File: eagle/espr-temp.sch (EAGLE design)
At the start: 34 parts, among them IC1 FT231XS-R, IC2 ESP-WROOM-02, IC3 AM2320

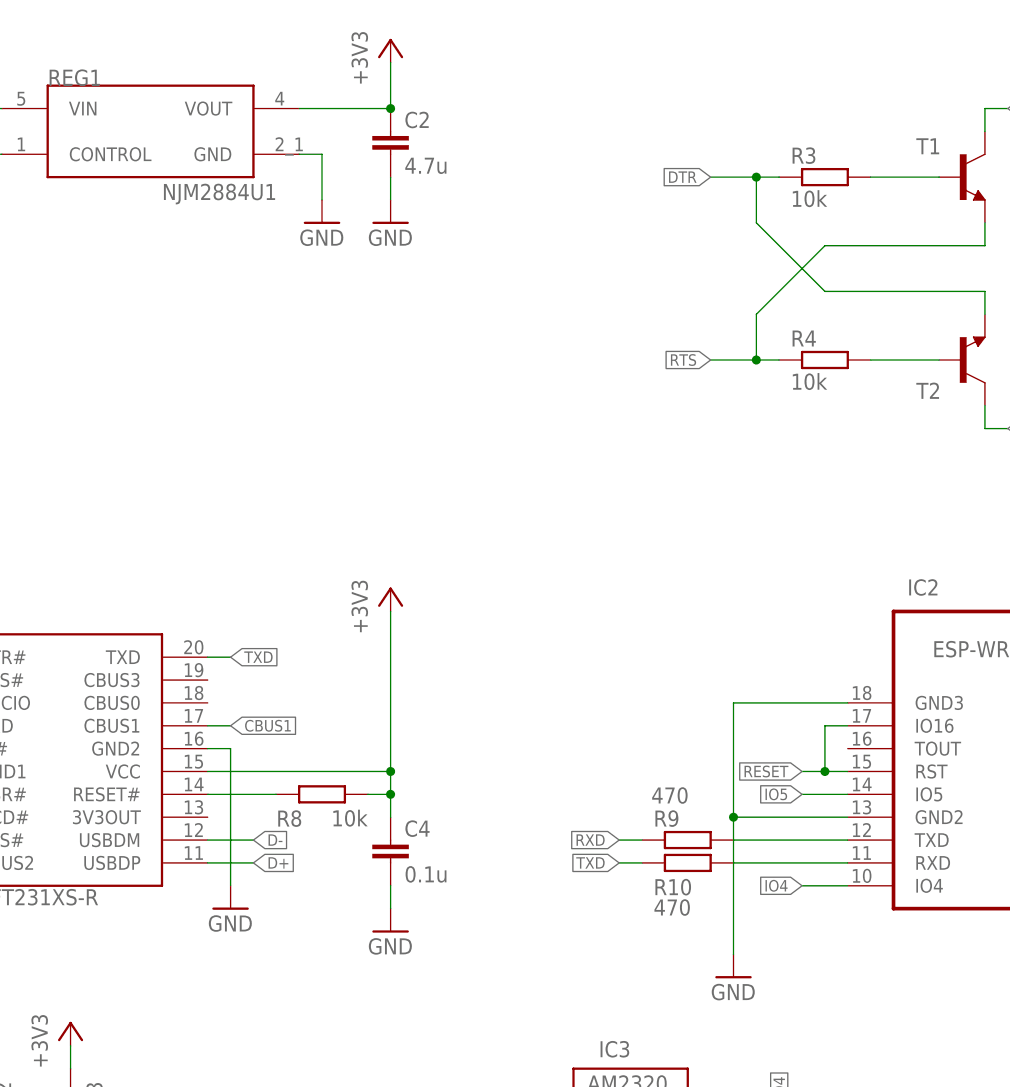
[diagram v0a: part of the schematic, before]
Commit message: fix some ERC errors
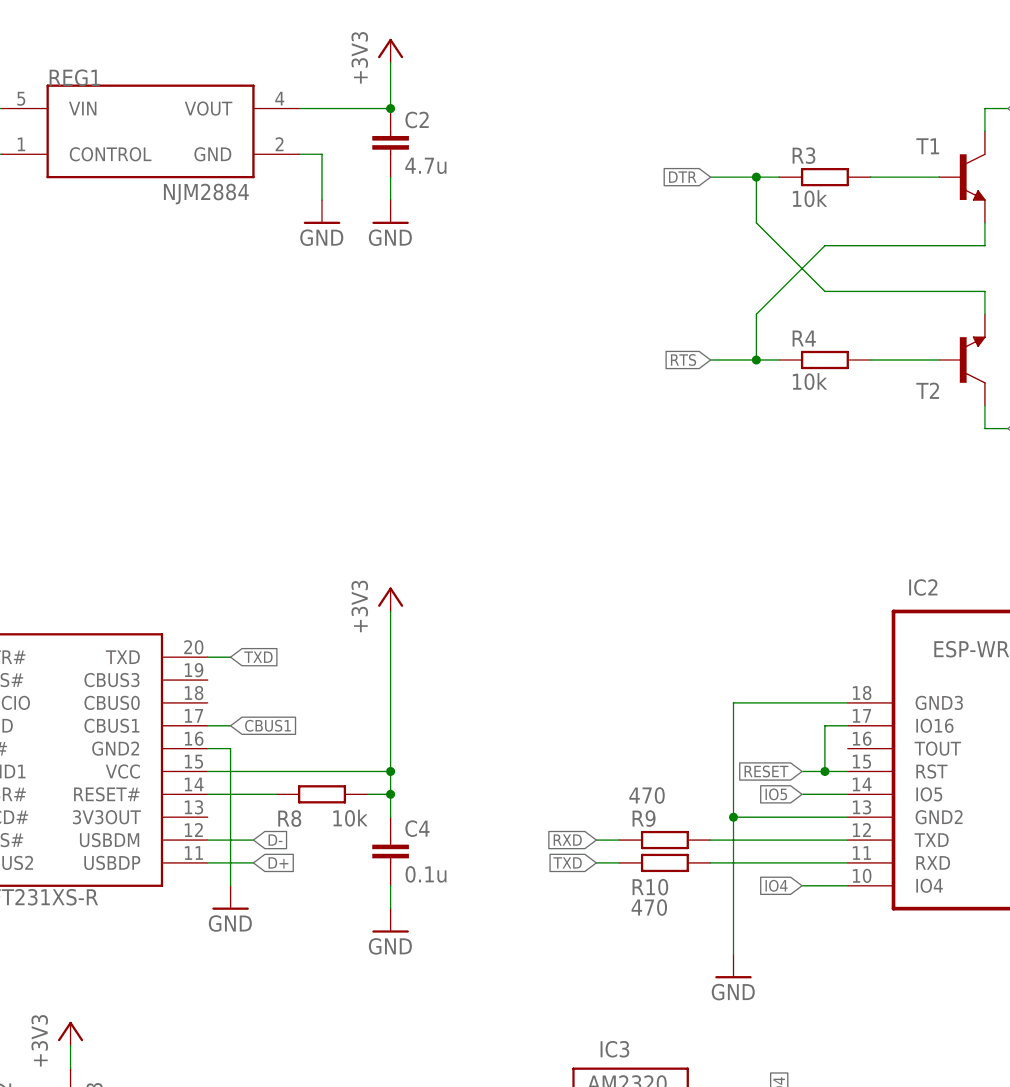
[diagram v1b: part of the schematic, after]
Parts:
- REG1: value NJM2884U1 -> NJM2884; device regulator:NJM2884U1 -> regulator:NJM2884
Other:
- moved on the sheet: R10, R9, REG1
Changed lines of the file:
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@@
 <part name="+3V32" library="supply1" library_urn="urn:adsk.eagle:library:371" deviceset="+3V3" device=""/>
 <part name="+3V33" library="supply1" library_urn="urn:adsk.eagle:library:371" deviceset="+3V3" device=""/>
-<part name="FRAME1" library="frames" library_urn="urn:adsk.eagle:library:229" deviceset="A4L-LOC" device=""/>
-<part name="REG1" library="regulator" deviceset="NJM2884U1" device=""/>
+<part name="FRAME1" library="frames" library_urn="urn:adsk.eagle:library:229" deviceset="A4L-LOC" device="" value="Frame"/>
+<part name="REG1" library="regulator" deviceset="NJM2884" device=""/>
 </parts>
 <sheets>
@@
 <attribute name="VALUE" x="58.674" y="13.081" size="1.778" layer="96"/>
 </instance>
-<instance part="R9" gate="G$1" x="10.16" y="-15.24" smashed="yes">
-<attribute name="NAME" x="6.35" y="-13.7414" size="1.778" layer="95"/>
-<attribute name="VALUE" x="6.096" y="-11.176" size="1.778" layer="96"/>
+<instance part="R9" gate="G$1" x="7.62" y="-15.24" smashed="yes">
+<attribute name="NAME" x="3.81" y="-13.7414" size="1.778" layer="95"/>
+<attribute name="VALUE" x="3.556" y="-11.176" size="1.778" layer="96"/>
 </instance>
 <instance part="R3" gate="G$1" x="25.4" y="58.42"/>
 <instance part="R4" gate="G$1" x="25.4" y="38.1"/>
-<instance part="R10" gate="G$1" x="10.16" y="-17.78" smashed="yes">
-<attribute name="NAME" x="6.35" y="-21.3614" size="1.778" layer="95"/>
-<attribute name="VALUE" x="6.35" y="-23.622" size="1.778" layer="96"/>
+<instance part="R10" gate="G$1" x="7.62" y="-17.78" smashed="yes">
+<attribute name="NAME" x="3.81" y="-21.3614" size="1.778" layer="95"/>
+<attribute name="VALUE" x="3.81" y="-23.622" size="1.778" layer="96"/>
 </instance>
 <instance part="GND1" gate="1" x="-30.48" y="53.34"/>
@@
 <segment>
 <pinref part="R10" gate="G$1" pin="1"/>
-<wire x1="5.08" y1="-17.78" x2="2.54" y2="-17.78" width="0.1524" layer="91"/>
-<label x="2.54" y="-17.78" size="1.27" layer="95" rot="R180" xref="yes"/>
+<wire x1="2.54" y1="-17.78" x2="0" y2="-17.78" width="0.1524" layer="91"/>
+<label x="0" y="-17.78" size="1.27" layer="95" rot="R180" xref="yes"/>
 </segment>
 </net>
@@
 <segment>
 <pinref part="R9" gate="G$1" pin="1"/>
-<wire x1="5.08" y1="-15.24" x2="2.54" y2="-15.24" width="0.1524" layer="91"/>
-<label x="2.54" y="-15.24" size="1.27" layer="95" rot="R180" xref="yes"/>
+<wire x1="2.54" y1="-15.24" x2="0" y2="-15.24" width="0.1524" layer="91"/>
+<label x="0" y="-15.24" size="1.27" layer="95" rot="R180" xref="yes"/>
 </segment>
 </net>
@@
 <pinref part="R9" gate="G$1" pin="2"/>
 <pinref part="IC2" gate="G$1" pin="TXD"/>
-<wire x1="15.24" y1="-15.24" x2="27.94" y2="-15.24" width="0.1524" layer="91"/>
+<wire x1="12.7" y1="-15.24" x2="27.94" y2="-15.24" width="0.1524" layer="91"/>
 </segment>
 </net>
@@
 <pinref part="R10" gate="G$1" pin="2"/>
 <pinref part="IC2" gate="G$1" pin="RXD"/>
-<wire x1="15.24" y1="-17.78" x2="27.94" y2="-17.78" width="0.1524" layer="91"/>
-</segment>
-</net>
+<wire x1="12.7" y1="-17.78" x2="27.94" y2="-17.78" width="0.1524" layer="91"/>
+</segment>
+</net>

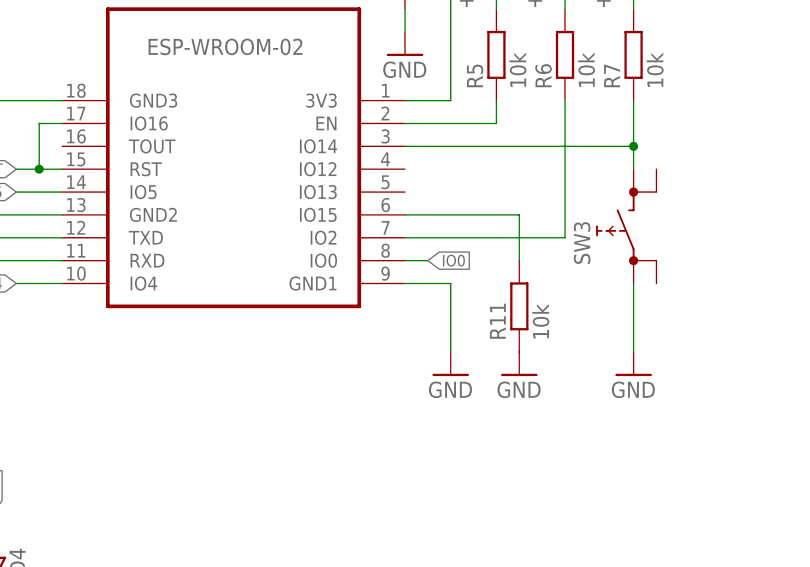
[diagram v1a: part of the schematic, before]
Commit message: change to GND from tRistrict for WROOM2 library
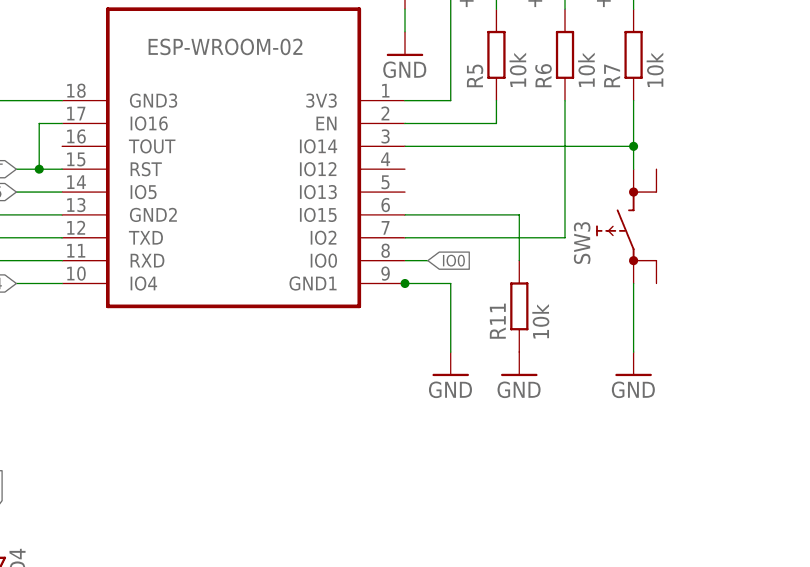
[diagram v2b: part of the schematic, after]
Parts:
- IC2: device esp-wroom-02:ESP-WROOM-02FRONT-FACE -> esp-wroom-02:ESP-WROOM-02
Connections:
- net GND: now also IC2.GND0
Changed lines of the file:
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@@
 <part name="GND14" library="supply1" library_urn="urn:adsk.eagle:library:371" deviceset="GND" device=""/>
 <part name="LED3" library="led-smd" deviceset="OSYL1608" device=""/>
-<part name="IC2" library="esp-wroom-02" deviceset="ESP-WROOM-02" device="FRONT-FACE" value="ESP-WROOM-02"/>
+<part name="IC2" library="esp-wroom-02" deviceset="ESP-WROOM-02" device="" value="ESP-WROOM-02"/>
 <part name="IC1" library="FT231XS-R" deviceset="FT231XS-R" device=""/>
 <part name="R8" library="registors" deviceset="R1608" device="" value="10k"/>
@@
 <pinref part="GND11" gate="1" pin="GND"/>
 <wire x1="71.12" y1="-20.32" x2="71.12" y2="-27.94" width="0.1524" layer="91"/>
-</segment>
-<segment>
+<pinref part="IC2" gate="G$1" pin="GND0"/>
+<junction x="66.04" y="-20.32"/>
+</segment>
+<segment>
